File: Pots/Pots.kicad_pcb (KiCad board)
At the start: 2 copper layers, 55 x 42.5 mm, 10 parts, among them J101 Conn_02x05_Odd_Even

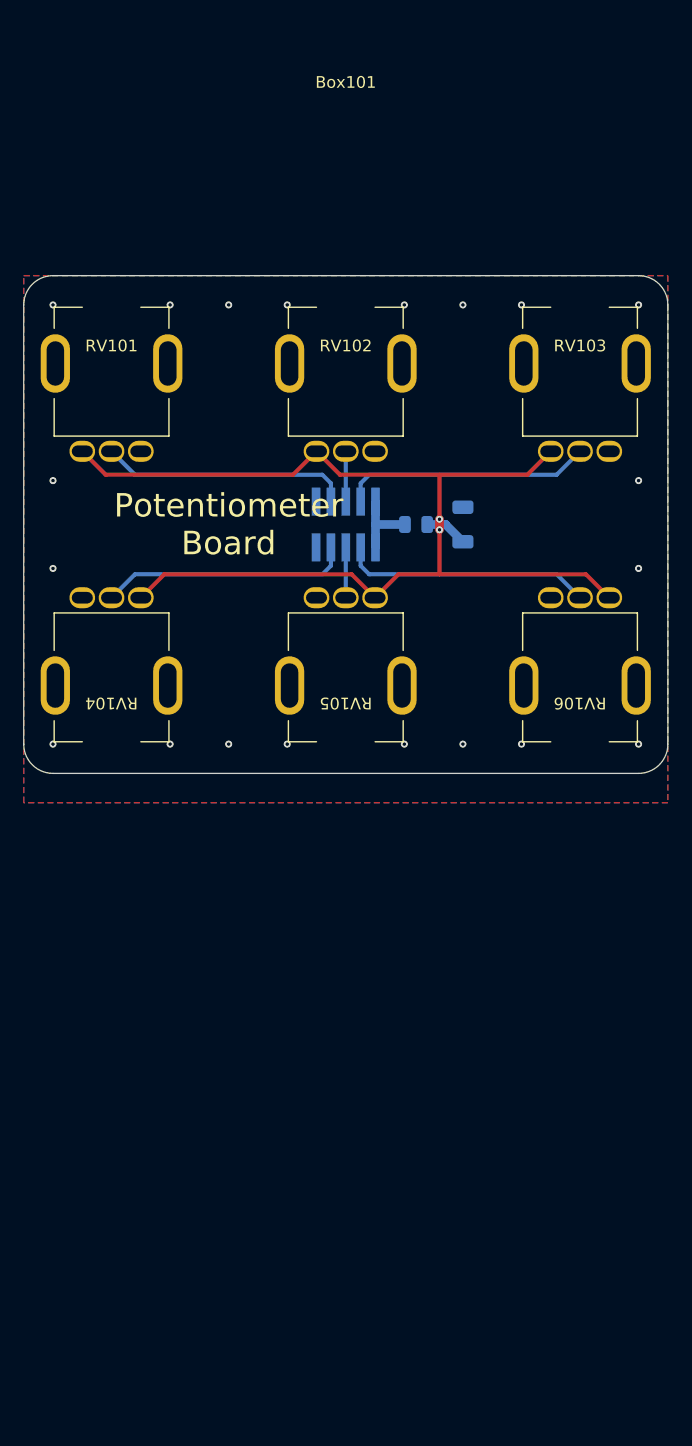
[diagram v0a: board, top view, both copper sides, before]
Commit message: Move 3d models to footprint directory
I tried to deal with the kicad path handling with a 'TOPLEVEL'
environment variable, but it worked horribly badly and got out of sync
because kicad didn't really integrate very well with it.

So just live with the fact that you can only have per-project paths for
the symbol and footprint libraries, not for the 3D models.  kicad does
have the notion of "3D model paths", but they aren't per project.

It looks like the way to keep kicad happy and avoid too much confusion
is to just make the 3D models be part of the footprint library, and put
the STEP files in the same path.  I'll keep the original openscad models
in the 'Models' (and 'Enclosures') directories.

Let's see if this fixes my issues.

Also, this mixes in various other edits to the 1590B footprint in
particular, since I couldn't keep the regularly scheduled kicad noise
separate from the 'move things around' noise.  kicad likes to randomly
update the uuid's of various parts as something changes (or, as I
sometimes feel, even if nothing changes).

So this is not a particularly clean commit: this also moves the pot
locations up by 5mm in the 1590B enclosure because that's what I was
looking at when the potentiometer board stopped showing 3d models due to
path confusion.

Signed-off-by: Linus Torvalds <torvalds@linux-foundation.org>
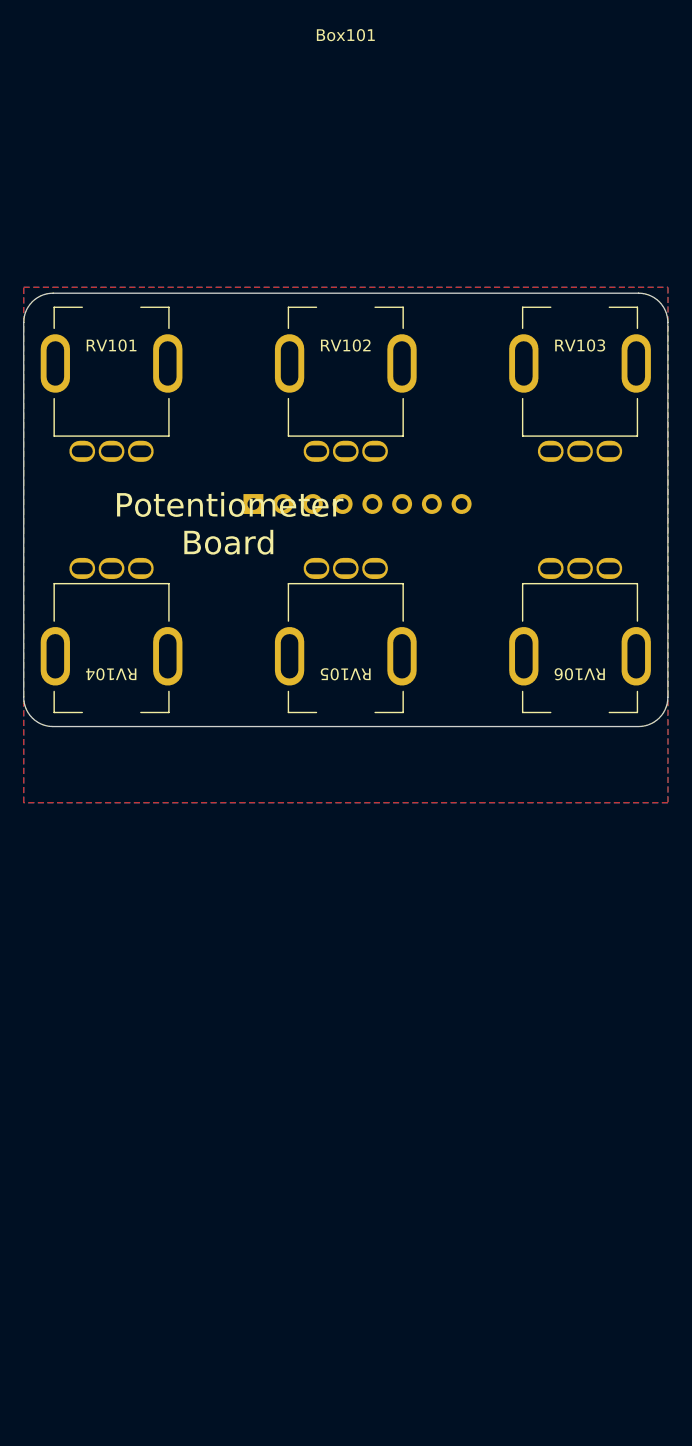
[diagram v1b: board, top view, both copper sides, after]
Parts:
- removed C101: 22uF, Capacitor_SMD:C_1206_3216Metric
- removed R101: 220R, Capacitor_SMD:C_0805_2012Metric
- Box101: value 125B -> 1590B; footprint Mylib:125B -> Mylib:1590B
- J101: value Conn_02x05_Odd_Even -> Conn_01x08_Pin; footprint Connector_PinHeader_1.27mm:PinHeader_2x05_P1.27mm_Vertical_SMD -> Connector_PinHeader_2.54mm:PinHeader_1x08_P2.54mm_Vertical
- moved J101 8.08 mm to (92.1, 72.0), turned to -90 degrees
- moved RV104 2.50 mm to (80.0, 85.0)
- moved RV105 2.50 mm to (100.0, 85.0)
- moved RV106 2.50 mm to (120.0, 85.0)
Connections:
- J101 pad 2: VIN -> POT1
- J101 pad 3: POT6 -> POT2
- J101 pad 5: POT5 -> POT4
- J101 pad 6: POT2 -> POT5
- J101 pad 7: POT4 -> POT6
- J101 pad 8: POT1 -> GND
- RV101 pad 1: +VA -> VIN
- RV102 pad 1: +VA -> VIN
- RV103 pad 1: +VA -> VIN
- RV104 pad 1: +VA -> VIN
- RV105 pad 1: +VA -> VIN
- RV106 pad 1: +VA -> VIN
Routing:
- net +VA: track 100.0 -> 0.00 mm, vias 2 -> 0
- net POT6: track 21.4 -> 0.00 mm
- net POT4: track 21.4 -> 0.00 mm
- net POT3: track 21.4 -> 0.00 mm
- net POT1: track 21.4 -> 0.00 mm
- net VIN: track 6.41 -> 0.00 mm
- net POT5: track 4.30 -> 0.00 mm
- net POT2: track 4.30 -> 0.00 mm
- net GND: vias 20 -> 0
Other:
- board size 55 x 42.5 mm -> 55 x 37 mm

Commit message: Update potentiometer board
I think I have decided on 2x04 connector to the potentiometer board, at
least for now.  It's a bit more mechanically stable than a 1x08.

So redo the routing, do some via stitching, and put that thing in the
middle of the potentiometer board.  I think I'm almost ready for a 1590B
Daisy Seed board.

Signed-off-by: Linus Torvalds <torvalds@linux-foundation.org>
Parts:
- removed J101: Conn_01x08_Pin, Connector_PinHeader_2.54mm:PinHeader_1x08_P2.54mm_Vertical
- added J201: Conn_02x04_Odd_Even, Connector_PinSocket_2.54mm:PinSocket_2x04_P2.54mm_Vertical, B.Cu at (103.8, 71.2)
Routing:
- net VIN: track 0.00 -> 115.3 mm
- net POT1: track 0.00 -> 25.4 mm
- net POT4: track 0.00 -> 23.9 mm
- net POT6: track 0.00 -> 22.8 mm
- net POT3: track 0.00 -> 21.3 mm
- net POT2: track 0.00 -> 8.88 mm
- net POT5: track 0.00 -> 6.80 mm
- net GND: vias 0 -> 44

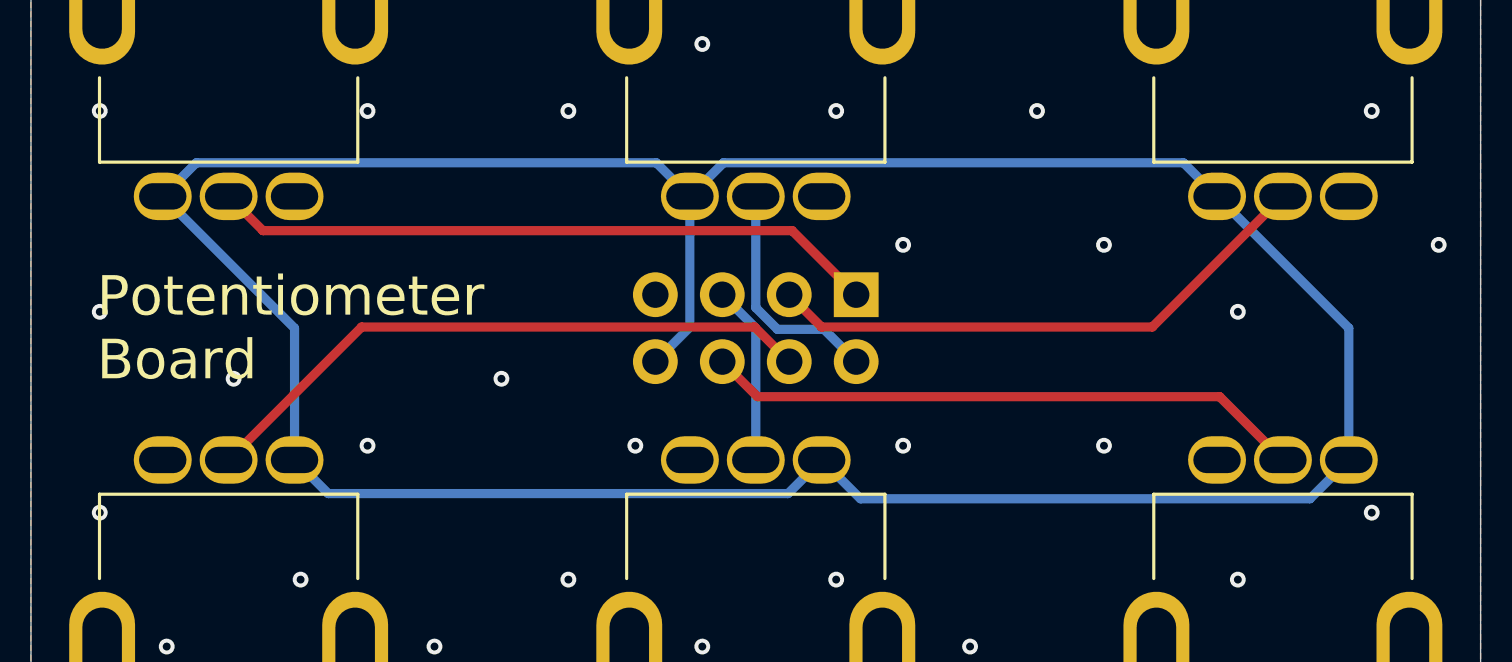
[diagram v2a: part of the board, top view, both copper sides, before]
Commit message: Switch pots around for sane behavior
My 1590B test board works fine, but I was confused about the behavior of
the pots.  It turns out that for about the fifteenth time, I had them
the wrong way around.

Obviously the real cause is my incompetence, but I think it's made worse
by how the default symbol is laid out, with pin 1 at the top.  I then
mindlessly hook it up with positive rail at the top and ground at the
bottom, and the end result is the opposite of what the trivial
expectation is.

Not a biggie, this doesn't matter for my testing and could have been
fixed by just reprogramming the Daisy Seed too, but it's obviously a
"D'oh" moment.

Signed-off-by: Linus Torvalds <torvalds@linux-foundation.org>
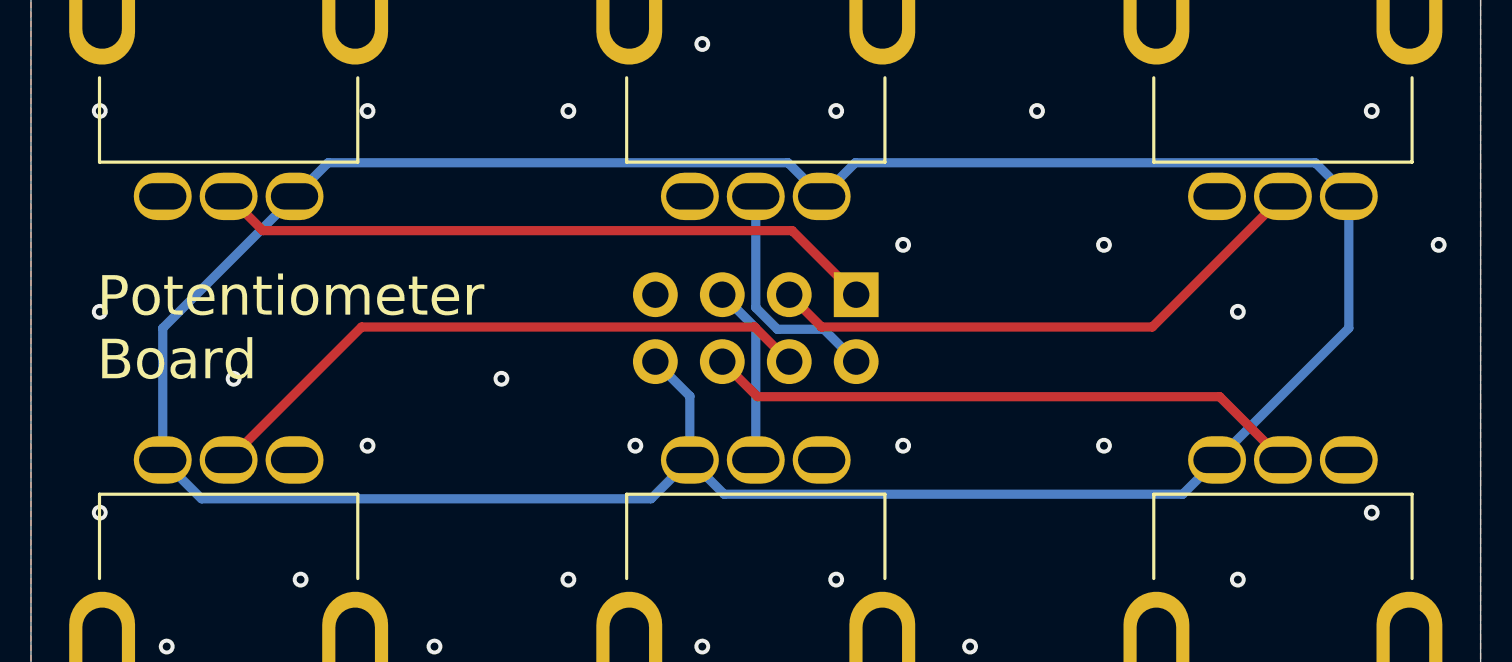
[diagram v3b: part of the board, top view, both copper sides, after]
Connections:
- RV101 pad 1: VIN -> GND
- RV101 pad 3: GND -> VIN
- RV102 pad 1: VIN -> GND
- RV102 pad 3: GND -> VIN
- RV103 pad 1: VIN -> GND
- RV103 pad 3: GND -> VIN
- RV104 pad 1: VIN -> GND
- RV104 pad 3: GND -> VIN
- RV105 pad 1: VIN -> GND
- RV105 pad 3: GND -> VIN
- RV106 pad 1: VIN -> GND
- RV106 pad 3: GND -> VIN
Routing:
- net VIN: track 115.3 -> 112.8 mm
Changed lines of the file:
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@@
 			(layers "*.Cu" "*.Mask")
 			(remove_unused_layers no)
-			(net 7 "VIN")
+			(net 1 "GND")
 			(pinfunction "1")
 			(pintype "passive")
@@
 			(layers "*.Cu" "*.Mask")
 			(remove_unused_layers no)
-			(net 1 "GND")
+			(net 7 "VIN")
 			(pinfunction "3")
 			(pintype "passive")
@@
 			(layers "*.Cu" "*.Mask")
 			(remove_unused_layers no)
-			(net 7 "VIN")
+			(net 1 "GND")
 			(pinfunction "1")
 			(pintype "passive")
@@
 			(layers "*.Cu" "*.Mask")
 			(remove_unused_layers no)
-			(net 1 "GND")
+			(net 7 "VIN")
 			(pinfunction "3")
 			(pintype "passive")
@@
 			(layers "*.Cu" "*.Mask")
 			(remove_unused_layers no)
-			(net 7 "VIN")
+			(net 1 "GND")
 			(pinfunction "1")
 			(pintype "passive")
@@
 			(layers "*.Cu" "*.Mask")
 			(remove_unused_layers no)
-			(net 1 "GND")
+			(net 7 "VIN")
 			(pinfunction "3")
 			(pintype "passive")
@@
 			(layers "*.Cu" "*.Mask")
 			(remove_unused_layers no)
-			(net 7 "VIN")
+			(net 1 "GND")
 			(pinfunction "1")
 			(pintype "passive")
@@
 			(layers "*.Cu" "*.Mask")
 			(remove_unused_layers no)
-			(net 1 "GND")
+			(net 7 "VIN")
 			(pinfunction "3")
 			(pintype "passive")
@@
 			(layers "*.Cu" "*.Mask")
 			(remove_unused_layers no)
-			(net 7 "VIN")
+			(net 1 "GND")
 			(pinfunction "1")
 			(pintype "passive")
@@
 			(layers "*.Cu" "*.Mask")
 			(remove_unused_layers no)
-			(net 1 "GND")
+			(net 7 "VIN")
 			(pinfunction "3")
 			(pintype "passive")
@@
 			(layers "*.Cu" "*.Mask")
 			(remove_unused_layers no)
-			(net 7 "VIN")
+			(net 1 "GND")
 			(pinfunction "1")
 			(pintype "passive")
@@
 			(layers "*.Cu" "*.Mask")
 			(remove_unused_layers no)
-			(net 1 "GND")
+			(net 7 "VIN")
 			(pinfunction "3")
 			(pintype "passive")
@@
 	)
 	(segment
-		(start 102.5 77.5)
-		(end 101.224 78.776)
+		(start 116.2 78.8)
+		(end 117.5 77.5)
 		(width 0.35)
 		(layer "B.Cu")
@@
 	)
 	(segment
-		(start 97.5 67.5)
-		(end 98.776 66.224)
+		(start 96.19 73.77)
+		(end 97.5 75.08)
 		(width 0.35)
 		(layer "B.Cu")
@@
 	)
 	(segment
-		(start 101.224 78.776)
-		(end 83.776 78.776)
+		(start 83.776 66.224)
+		(end 82.5 67.5)
 		(width 0.35)
 		(layer "B.Cu")
@@
 	)
 	(segment
-		(start 122.5 72.5)
-		(end 117.5 67.5)
+		(start 122.5 67.5)
+		(end 121.224 66.224)
 		(width 0.35)
 		(layer "B.Cu")
@@
 	)
 	(segment
-		(start 116.224 66.224)
-		(end 117.5 67.5)
+		(start 78.974 78.974)
+		(end 77.5 77.5)
 		(width 0.35)
 		(layer "B.Cu")
@@
 	)
 	(segment
-		(start 98.776 66.224)
-		(end 116.224 66.224)
+		(start 97.5 77.5)
+		(end 96.026 78.974)
 		(width 0.35)
 		(layer "B.Cu")
@@
 	)
 	(segment
-		(start 121.026 78.974)
-		(end 103.974 78.974)
+		(start 77.5 72.5)
+		(end 77.5 77.5)
 		(width 0.35)
 		(layer "B.Cu")
@@
 	)
 	(segment
-		(start 83.776 78.776)
-		(end 82.5 77.5)
+		(start 97.5 77.5)
+		(end 98.8 78.8)
 		(width 0.35)
 		(layer "B.Cu")
@@
 	)
 	(segment
-		(start 78.776 66.224)
-		(end 96.224 66.224)
+		(start 102.5 67.5)
+		(end 101.224 66.224)
 		(width 0.35)
 		(layer "B.Cu")
@@
 	)
 	(segment
-		(start 82.5 72.5)
-		(end 77.5 67.5)
+		(start 121.224 66.224)
+		(end 103.776 66.224)
 		(width 0.35)
 		(layer "B.Cu")
@@
 	)
 	(segment
-		(start 122.5 77.5)
-		(end 122.5 72.5)
+		(start 101.224 66.224)
+		(end 83.776 66.224)
 		(width 0.35)
 		(layer "B.Cu")
@@
 	)
 	(segment
-		(start 82.5 77.5)
-		(end 82.5 72.5)
+		(start 98.8 78.8)
+		(end 116.2 78.8)
 		(width 0.35)
 		(layer "B.Cu")
@@
 	)
 	(segment
-		(start 96.224 66.224)
-		(end 97.5 67.5)
+		(start 96.026 78.974)
+		(end 78.974 78.974)
 		(width 0.35)
 		(layer "B.Cu")
@@
 	)
 	(segment
-		(start 77.5 67.5)
-		(end 78.776 66.224)
+		(start 103.776 66.224)
+		(end 102.5 67.5)
 		(width 0.35)
 		(layer "B.Cu")
@@
 	)
 	(segment
-		(start 103.974 78.974)
-		(end 102.5 77.5)
+		(start 97.5 75.08)
+		(end 97.5 77.5)
 		(width 0.35)
 		(layer "B.Cu")
@@
 	)
 	(segment
-		(start 122.5 77.5)
-		(end 121.026 78.974)
+		(start 122.5 72.5)
+		(end 117.5 77.5)
 		(width 0.35)
 		(layer "B.Cu")
@@
 	)
 	(segment
-		(start 97.5 72.46)
-		(end 97.5 67.5)
+		(start 82.5 67.5)
+		(end 77.5 72.5)
 		(width 0.35)
 		(layer "B.Cu")
@@
 	)
 	(segment
-		(start 96.19 73.77)
-		(end 97.5 72.46)
+		(start 122.5 67.5)
+		(end 122.5 72.5)
 		(width 0.35)
 		(layer "B.Cu")
